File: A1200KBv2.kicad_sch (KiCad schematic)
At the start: 101 parts, among them J1 Conn_01x32_Female, K1 ESC, K10 L.BLANK, K11 F1, K12 L.AMIGA, K13 2, K14 W, K15 A, K16 Z, K17 F2, K18 3, K19 E, K2 TILDE, K20 S, K21 X, K22 F3, K23 4, K24 R, K25 D, K26 C, K27 F4, K28 5, K29 T, K3 TAB, K30 F, K31 V, K32 SPACE SWITCH, K33 F5, K34 6, K35 Y, K36 G, K37 B, K38 7, K39 U, K4 CTRL, K40 H, K41 N, K42 F6, K43 8, K44 I, K45 J, K46 M, K47 9, K48 O, K49 K, K5 L.SHIFT, K50 LESSTHAN, K51 F7, K52 0, K53 P, K54 L, K55 GRTRTHAN, K56 F8, K57 MINUS, K58 L.CURLY, K59 COLON, K6 L.ALT, K60 QUESTION, K61 R.AMIGA, K62 F9, K63 PLUS, K64 R.CURLY, K65 ", K66 R.SHIFT, K67 R.ALT, K68 F10, K69 PIPE, K7 1, K70 R.BLANK, K71 RETURN, K72 BS, K73 LEFT, K74 DEL, K75 UP, K76 DOWN, K77 HELP, K78 RIGHT, K79 NUM_(, K8 Q, K80 NUM_7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

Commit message: New version with new footprints; low-profile plate stabilizers
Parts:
- K3, K83, K96: footprint key-switches.pretty-0.11.0:SW_Gateron_LowProfile_THT -> Amiga_FFC:KS-33-2U-plate-stabilizer
- K32: footprint key-switches.pretty-0.11.0:SW_Gateron_LowProfile_THT -> Amiga_FFC:KS-33-Universal-Space
- K66: footprint key-switches.pretty-0.11.0:SW_Gateron_LowProfile_THT -> Amiga_FFC:KS-33-2.75U-plate-stabilizer
- K71: footprint key-switches.pretty-0.11.0:SW_Gateron_LowProfile_THT -> Amiga_FFC:KS-33-ISO-plate-stabilizer
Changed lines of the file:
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@@
 			)
 		)
-		(property "Footprint" "key-switches.pretty-0.11.0:SW_Gateron_LowProfile_THT"
+		(property "Footprint" "Amiga_FFC:KS-33-2U-plate-stabilizer"
 			(at 498.475 268.4018 0)
 			(effects
@@
 			)
 		)
-		(property "Footprint" "key-switches.pretty-0.11.0:SW_Gateron_LowProfile_THT"
+		(property "Footprint" "Amiga_FFC:KS-33-Universal-Space"
 			(at 176.53 268.4018 0)
 			(effects
@@
 			)
 		)
-		(property "Footprint" "key-switches.pretty-0.11.0:SW_Gateron_LowProfile_THT"
+		(property "Footprint" "Amiga_FFC:KS-33-2U-plate-stabilizer"
 			(at 561.975 253.1618 0)
 			(effects
@@
 			)
 		)
-		(property "Footprint" "key-switches.pretty-0.11.0:SW_Gateron_LowProfile_THT"
+		(property "Footprint" "Amiga_FFC:KS-33-ISO-plate-stabilizer"
 			(at 387.35 192.2018 0)
 			(effects
@@
 			)
 		)
-		(property "Footprint" "key-switches.pretty-0.11.0:SW_Gateron_LowProfile_THT"
+		(property "Footprint" "Amiga_FFC:KS-33-2U-plate-stabilizer"
 			(at 44.45 192.2018 0)
 			(effects
@@
 			)
 		)
-		(property "Footprint" "key-switches.pretty-0.11.0:SW_Gateron_LowProfile_THT"
+		(property "Footprint" "Amiga_FFC:KS-33-2.75U-plate-stabilizer"
 			(at 349.25 243.0018 0)
 			(effects

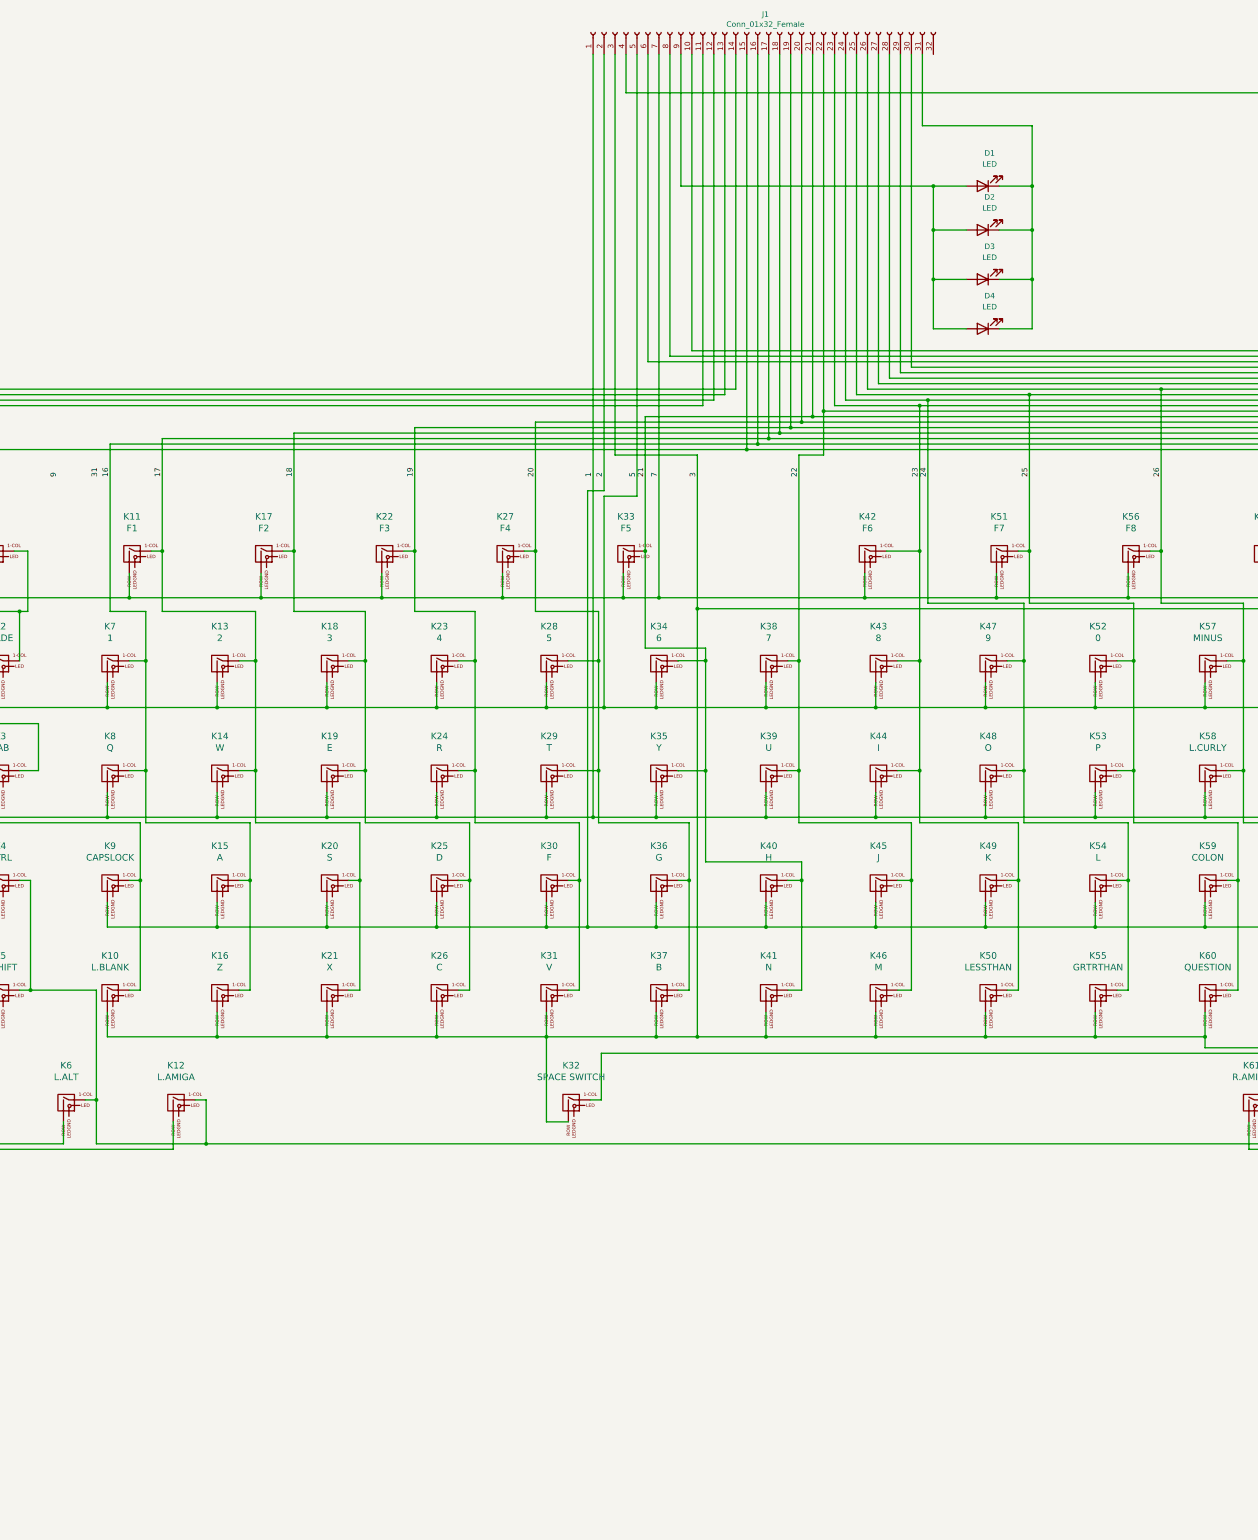
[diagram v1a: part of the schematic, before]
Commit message: fab 9/7/24 A1200 for KS-33 A1200.net case
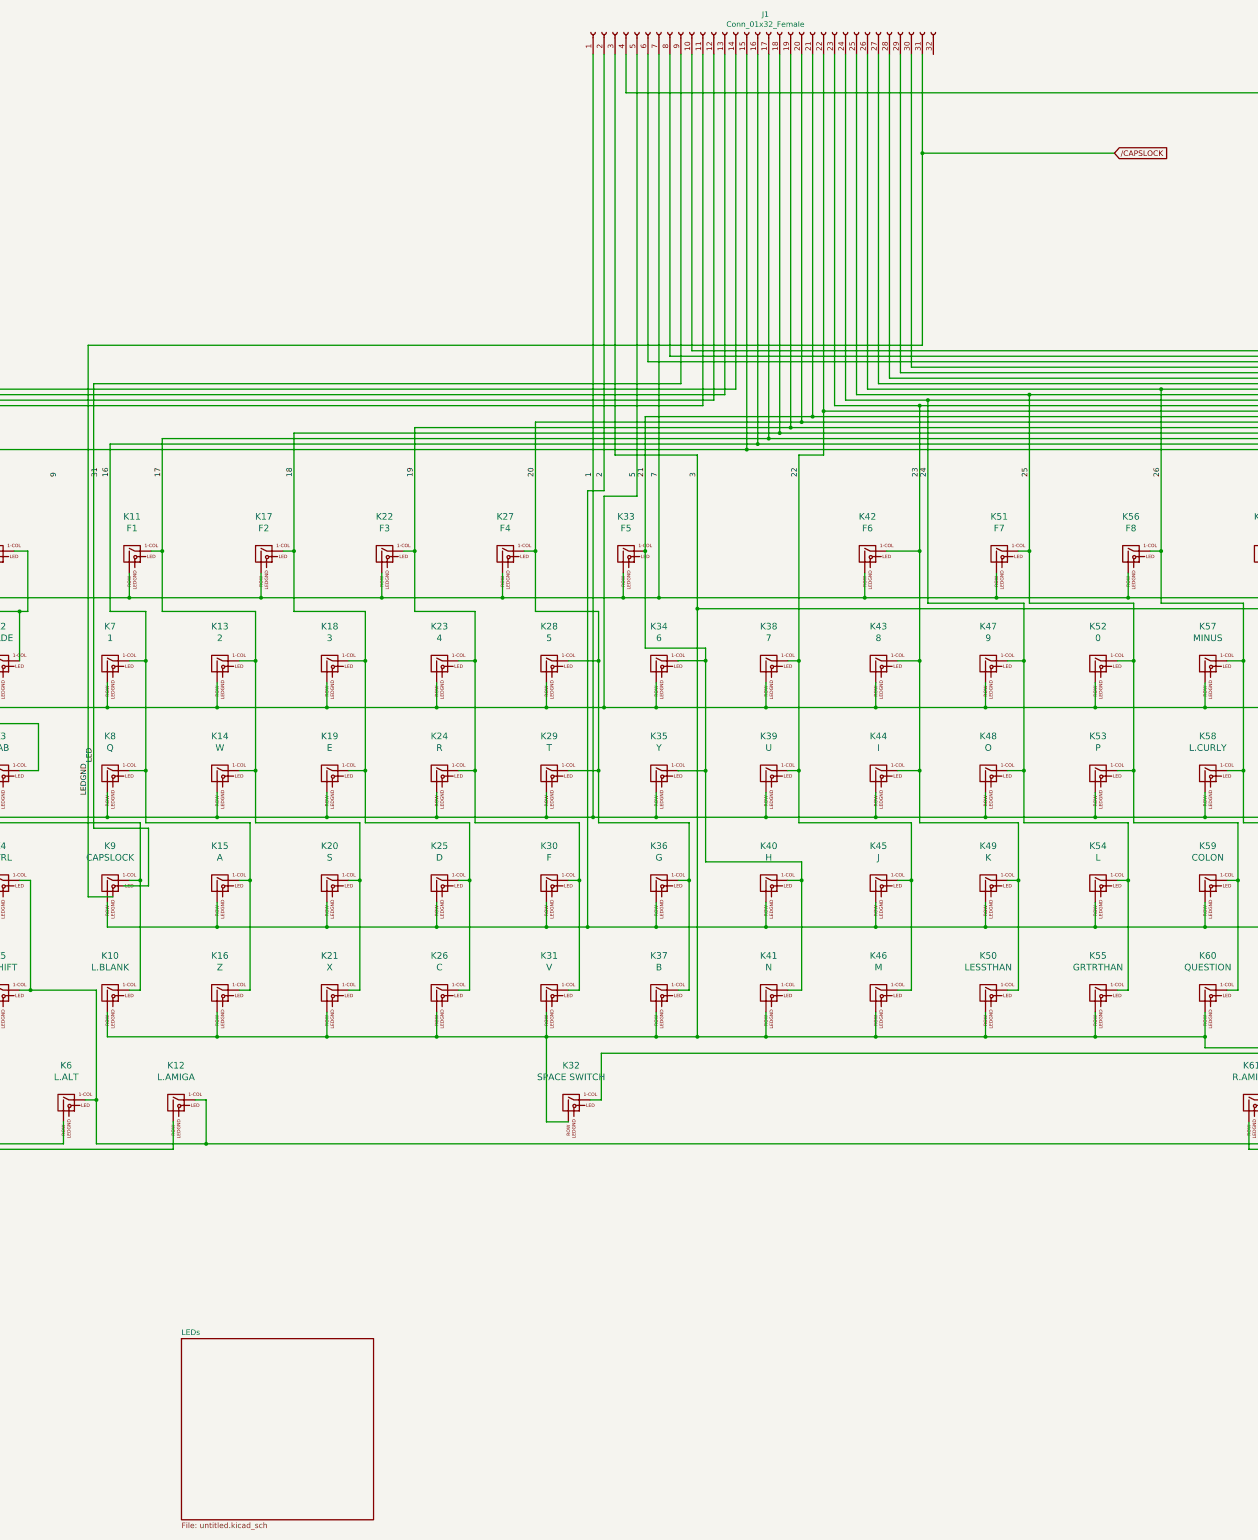
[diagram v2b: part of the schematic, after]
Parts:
- removed D1, D2, D3, D4: LED, LED_SMD:LED_0805_2012Metric_Pad1.15x1.40mm_HandSolder, symbol Device:LED
- K1, K10, K13, K14, K15, K16, K18, K19, K20, K21, K23, K24, K25, K26, K28, K29, K30, K31, K34, K35, K36, K37, K38, K39, K40, K41, K43, K44, K45, K46, K47, K48, K49, K50, K52, K53, K54, K55, K57, K58, K59, K60, K63, K64, K65, K69, K7, K70, K72, K73, K75, K76, K78, K79, K8, K80, K81, K82, K84, K85, K86, K87, K88, K89, K90, K91, K92, K93, K94, K95: footprint key-switches.pretty-0.11.0:SW_Gateron_LowProfile_THT -> Amiga Keyboard:Gateron-KS33-Solderable-1U
- K11, K12, K17, K22, K27, K33, K4, K42, K51, K56, K6, K61, K62, K67, K68: footprint key-switches.pretty-0.11.0:SW_Gateron_LowProfile_THT -> Amiga Keyboard:Gateron-KS33-Solderable-1.25U
- K2, K74, K77: footprint key-switches.pretty-0.11.0:SW_Gateron_LowProfile_THT -> Amiga Keyboard:Gateron-KS33-Solderable-1.5U
- K3, K83, K96: footprint Amiga_FFC:KS-33-2U-plate-stabilizer -> Amiga Keyboard:KS-33-2U-stabilizer
- K32: footprint Amiga_FFC:KS-33-Universal-Space -> Amiga Keyboard:KS-33-8U-space
- K5: footprint key-switches.pretty-0.11.0:SW_Gateron_LowProfile_THT -> Amiga Keyboard:Gateron-KS33-Solderable-1.75U
- K66: footprint Amiga_FFC:KS-33-2.75U-plate-stabilizer -> Amiga Keyboard:KS-33-2U-stabilizer
- K71: footprint Amiga_FFC:KS-33-ISO-plate-stabilizer -> Amiga Keyboard:KS-33-ISO-2U-stabilizer
- K9: footprint key-switches.pretty-0.11.0:SW_Gateron_LowProfile_THT -> Amiga Keyboard:Gateron-KS33-LED-Solderable-1U
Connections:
- net LED: now reaches K9.3 (LED)
- net LED: now also J1.9 (Pin_9)
- net /CAPSLOCK: now reaches K9.4 (LEDGND)
- net /CAPSLOCK: now also J1.31 (Pin_31)
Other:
- added sheet LEDs (untitled.kicad_sch)

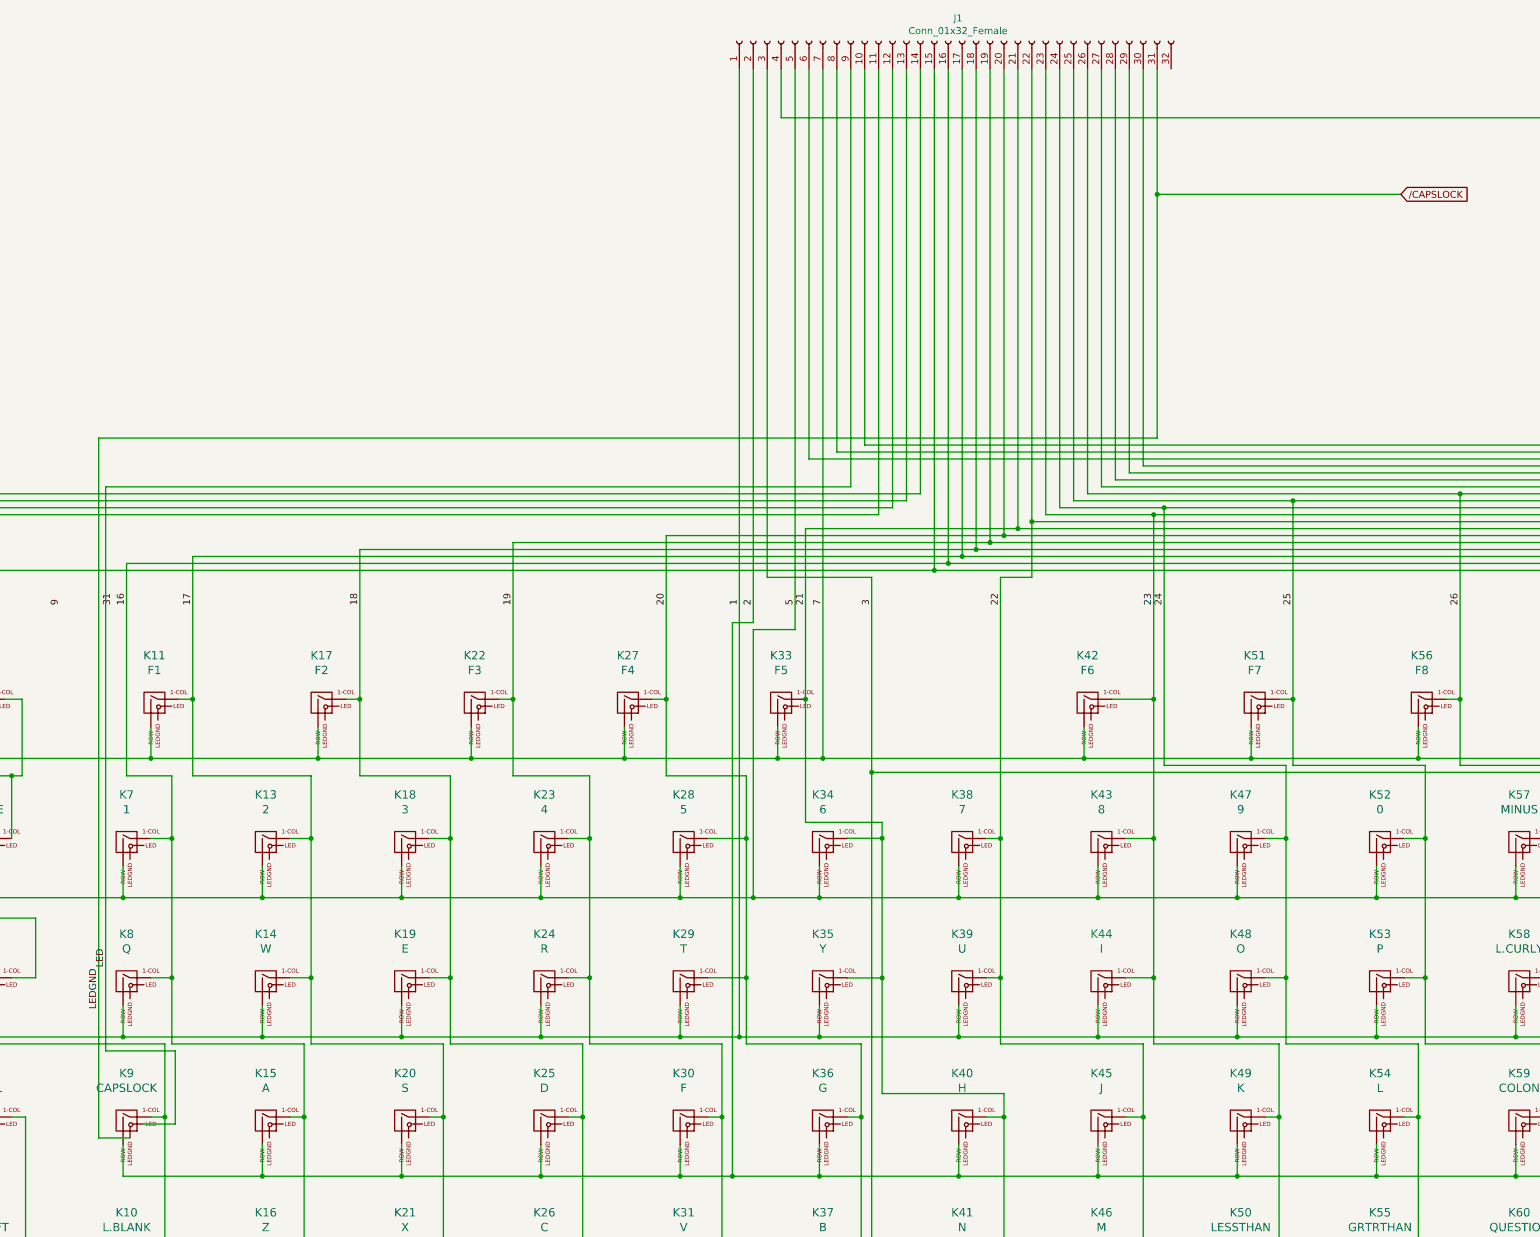
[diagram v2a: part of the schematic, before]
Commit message: Plates for final r5
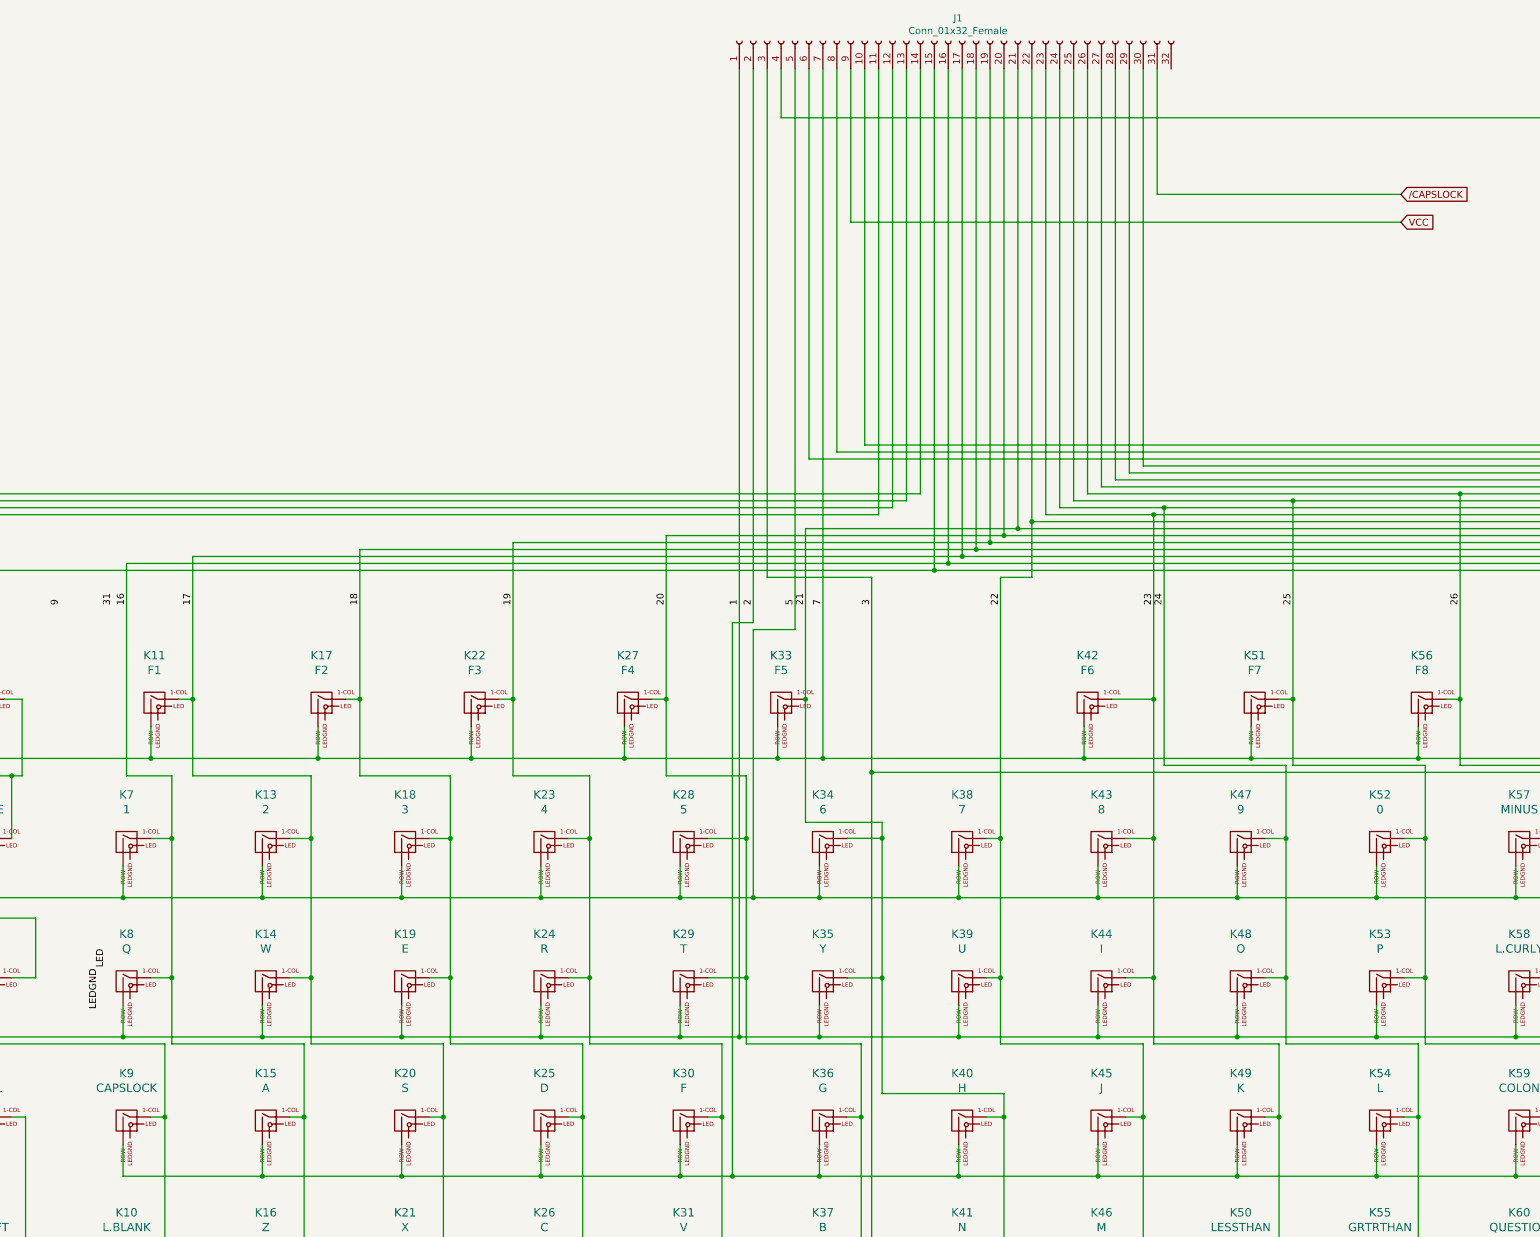
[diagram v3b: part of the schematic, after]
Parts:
- K9: footprint Amiga Keyboard:Gateron-KS33-LED-Solderable-1U -> Amiga Keyboard:Gateron-KS33-Solderable-1U
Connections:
- net LED: no longer J1.9 (Pin_9), K9.3 (LED)
- net /CAPSLOCK: no longer K9.4 (LEDGND)
- new net VCC: J1.9 (Pin_9)
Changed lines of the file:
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@@
 	)
 	(junction
-		(at 257.81 54.61)
-		(diameter 0)
-		(color 0 0 0 0)
-	)
-	(junction
 		(at 280.035 222.885)
 		(diameter 0)
@@
 	(wire
 		(pts
-			(xy 73.025 224.155) (xy 78.74 224.155)
-		)
-		(stroke
-			(width 0)
-			(type default)
-		)
-	)
-	(wire
-		(pts
 			(xy 242.57 110.49) (xy 242.57 31.75)
 		)
@@
 	(wire
 		(pts
-			(xy 78.74 224.155) (xy 78.74 210.82)
-		)
-		(stroke
-			(width 0)
-			(type default)
-		)
-	)
-	(wire
-		(pts
 			(xy 180.975 273.685) (xy 183.515 273.685)
 		)
@@
 	(wire
 		(pts
-			(xy 201.93 31.75) (xy 201.93 107.95)
-		)
-		(stroke
-			(width 0)
-			(type default)
-		)
-	)
-	(wire
-		(pts
 			(xy 552.45 273.685) (xy 552.45 116.84)
 		)
@@
 	(wire
 		(pts
-			(xy 70.485 226.695) (xy 64.77 226.695)
+			(xy 201.93 59.69) (xy 302.26 59.69)
 		)
 		(stroke
@@
 	(wire
 		(pts
-			(xy 64.77 99.06) (xy 64.77 226.695)
-		)
-		(stroke
-			(width 0)
-			(type default)
-		)
-	)
-	(wire
-		(pts
 			(xy 74.295 151.765) (xy 74.295 157.48)
 		)
@@
 	(wire
 		(pts
-			(xy 66.04 210.82) (xy 66.04 107.95)
-		)
-		(stroke
-			(width 0)
-			(type default)
-		)
-	)
-	(wire
-		(pts
 			(xy 403.86 182.88) (xy 403.86 233.045)
 		)
@@
 	(wire
 		(pts
-			(xy 257.81 54.61) (xy 257.81 99.06)
+			(xy 182.88 209.55) (xy 182.88 197.485)
 		)
 		(stroke
@@
 	(wire
 		(pts
-			(xy 182.88 209.55) (xy 182.88 197.485)
+			(xy 43.815 208.28) (xy 69.215 208.28)
 		)
 		(stroke
@@
 	(wire
 		(pts
-			(xy 43.815 208.28) (xy 69.215 208.28)
+			(xy 196.215 259.08) (xy 205.74 259.08)
 		)
 		(stroke
@@
 	(wire
 		(pts
-			(xy 196.215 259.08) (xy 205.74 259.08)
+			(xy 201.93 31.75) (xy 201.93 59.69)
 		)
 		(stroke
@@
 	(wire
 		(pts
-			(xy 257.81 99.06) (xy 64.77 99.06)
-		)
-		(stroke
-			(width 0)
-			(type default)
-		)
-	)
-	(wire
-		(pts
 			(xy 76.835 248.285) (xy 76.835 222.885)
 		)
@@
 	(wire
 		(pts
-			(xy 78.74 210.82) (xy 66.04 210.82)
-		)
-		(stroke
-			(width 0)
-			(type default)
-		)
-	)
-	(wire
-		(pts
 			(xy 221.615 202.565) (xy 221.615 208.28)
 		)
@@
 	(wire
 		(pts
-			(xy 66.04 107.95) (xy 201.93 107.95)
-		)
-		(stroke
-			(width 0)
-			(type default)
-		)
-	)
-	(wire
-		(pts
 			(xy 348.615 233.68) (xy 374.015 233.68)
 		)
@@
 		)
 	)
+	(global_label "VCC"
+		(shape input)
+		(at 302.26 59.69 0)
+		(fields_autoplaced yes)
+		(effects
+			(font
+				(size 1.27 1.27)
+			)
+			(justify left)
+		)
+		(property "Intersheetrefs" "${INTERSHEET_REFS}"
+			(at 308.8738 59.69 0)
+			(effects
+				(font
+					(size 1.27 1.27)
+				)
+				(justify left)
+				(hide yes)
+			)
+		)
+	)
 	(global_label "{slash}CAPSLOCK"
 		(shape input)
@@
 			)
 		)
-		(property "Footprint" "Amiga Keyboard:Gateron-KS33-LED-Solderable-1U"
+		(property "Footprint" "Amiga Keyboard:Gateron-KS33-Solderable-1U"
 			(at 69.85 217.6018 0)
 			(effects
